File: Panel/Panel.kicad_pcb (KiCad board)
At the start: 2 copper layers, 100 x 100 mm, 81 parts, among them J1 Conn_01x03, J10 Conn_01x02, J11 Conn_01x03, J12 Conn_01x03, J2 USB_C_Receptacle_USB2.0, J3 Conn_01x02, J4 Conn_02x06_Odd_Even, J5 Conn_01x07, J6 Conn_01x02, J7 Conn_01x02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

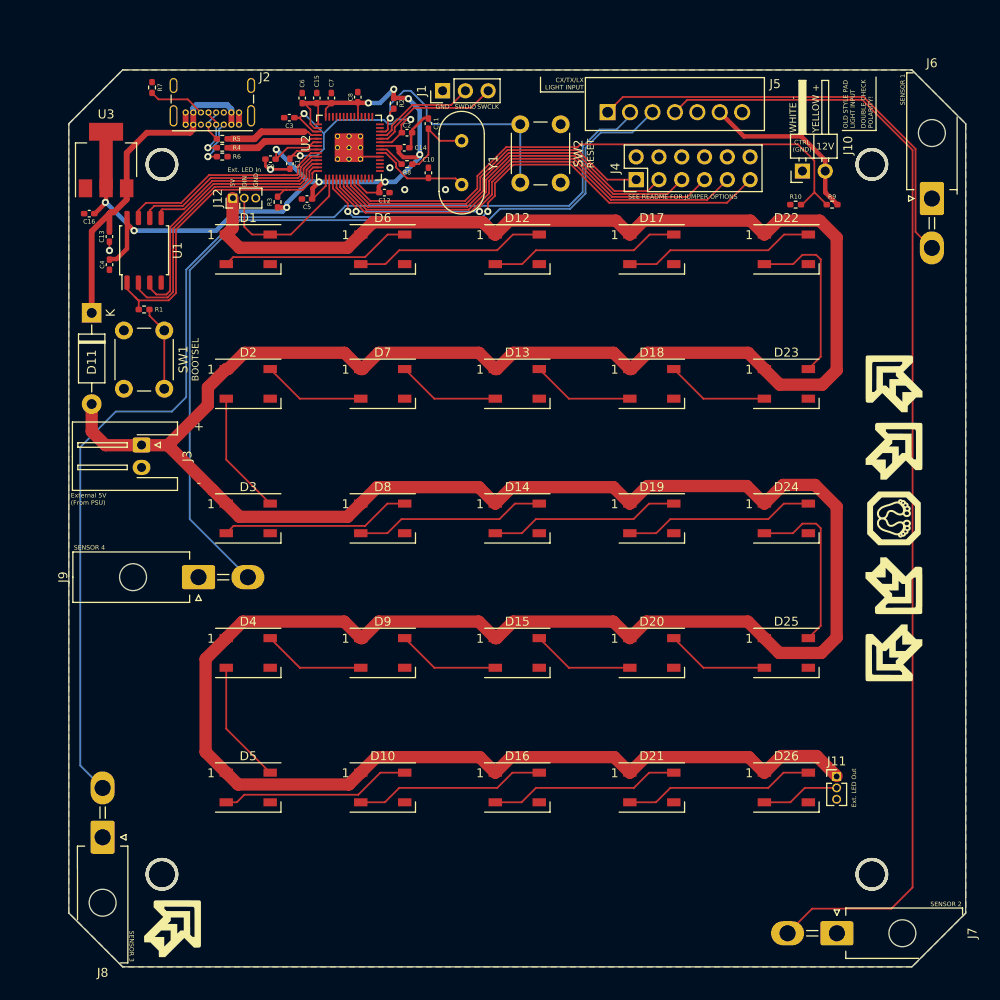
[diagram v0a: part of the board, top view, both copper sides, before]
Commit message: Add USB protection, GP25 LED, silkscreen tweaks
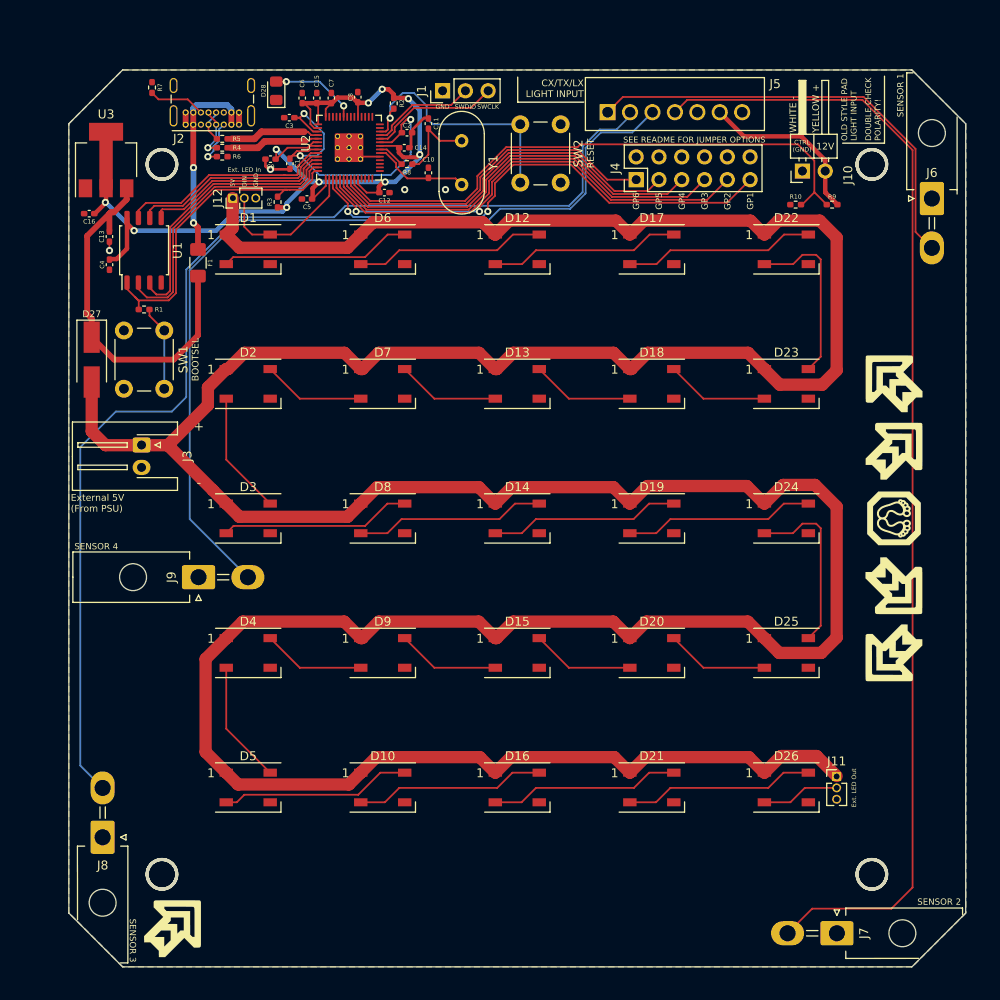
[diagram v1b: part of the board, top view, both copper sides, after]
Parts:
- removed D11: 1N4001, Diode_THT:D_DO-41_SOD81_P10.16mm_Horizontal
- added D27: SS34, Diode_SMD:D_SMA_Handsoldering, F.Cu at (82.5, 82.3)
- added D28: LED_Small, LED_SMD:LED_0805_2012Metric_Pad1.15x1.40mm_HandSolder, F.Cu at (103.1, 52.3)
- added F1: 500mA, Fuse:Fuse_1206_3216Metric_Pad1.42x1.75mm_HandSolder, F.Cu at (94.4, 71.5)
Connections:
- J2 pad A4: +5V -> Net-(J2-PadA4)
- J2 pad A9: +5V -> Net-(J2-PadA4)
- J2 pad B4: +5V -> Net-(J2-PadA4)
- J2 pad B9: +5V -> Net-(J2-PadA4)
- U2 pad 37: unconnected-(U2-Pad37) -> Net-(U2-Pad37)
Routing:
- net Net-(J2-PadA4): track 0.00 -> 22.3 mm, vias 0 -> 2
- net Net-(U2-Pad37): track 0.00 -> 9.87 mm, vias 0 -> 2
- net +1V1: track 32.3 -> 39.7 mm
- net +5V: track 39.0 -> 41.6 mm
- net Ext 5V: track 459.6 -> 462.1 mm
- net GND: vias 5 -> 4
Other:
- board text added: "GP1"
- board text added: "GP2"
- board text added: "GP3"
- board text added: "GP4"
- board text added: "GP5"
- board text added: "GP6"

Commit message: Enlarge mounting holes slightly
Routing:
- net SENSOR 1: track 49.2 -> 54.3 mm
- net SENSOR 2: track 127.6 -> 129.9 mm
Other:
- outline, holes or cut-outs redrawn
- board text added: "WHT"
- board text added: "YLW"
- board text removed: "CTRL (GND)"
- board text removed: "WHITE -"
- board text removed: "YELLOW +"
